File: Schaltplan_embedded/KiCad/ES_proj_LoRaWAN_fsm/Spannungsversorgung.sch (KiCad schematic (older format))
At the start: 37 parts, among them IC1 TLS850B0TBV33ATMA1, IC2 L6924D, IC3 TLS850B0TBV55ATMA1, IC4 SPV1040T, J2 CON-SOCJ-2155, J3 Conn_01x02_Female

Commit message: schaltplan neu
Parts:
- removed R4: 1k, Resistors_SMD:R_0805_HandSoldering, symbol Device:R
- removed R5: 68k, Resistors_SMD:R_0805_HandSoldering, symbol Device:R
- C15: footprint Capacitors_SMD:C_0603_HandSoldering -> Capacitors_SMD:CP_Elec_5x5.3
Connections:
- wire segments 169 -> 162
- no-connect marks 5 -> 6
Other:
- note removed: "Optional! Widerstände können\nevtl. noch weggelassen werden."
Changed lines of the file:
@@
 EESchema Schematic File Version 4
 LIBS:Schaltplan_embedded-cache
-EELAYER 26 0
+EELAYER 30 0
 EELAYER END
 $Descr A4 11693 8268
@@
 F 0 "C15" H 10418 5246 50  0000 L CNN
 F 1 "10uF" H 10418 5155 50  0000 L CNN
-F 2 "Capacitors_SMD:C_0603_HandSoldering" H 10338 5050 50  0001 C CNN
+F 2 "Capacitors_SMD:CP_Elec_5x5.3" H 10338 5050 50  0001 C CNN
 F 3 "~" H 10300 5200 50  0001 C CNN
 	1    10300 5200
@@
 $EndComp
 $Comp
-L Device:R R4
-U 1 1 5DD0CD69
-P 1150 3750
-F 0 "R4" V 943 3750 50  0000 C CNN
-F 1 "1k" V 1034 3750 50  0000 C CNN
-F 2 "Resistors_SMD:R_0805_HandSoldering" V 1080 3750 50  0001 C CNN
-F 3 "~" H 1150 3750 50  0001 C CNN
-	1    1150 3750
-	-1   0    0    1
-$EndComp
-$Comp
-L Device:R R5
-U 1 1 5DD0D292
-P 1150 4150
-F 0 "R5" V 943 4150 50  0000 C CNN
-F 1 "68k" V 1034 4150 50  0000 C CNN
-F 2 "Resistors_SMD:R_0805_HandSoldering" V 1080 4150 50  0001 C CNN
-F 3 "~" H 1150 4150 50  0001 C CNN
-	1    1150 4150
-	-1   0    0    1
-$EndComp
-$Comp
-L power:GND #PWR01
-U 1 1 5DD102DE
-P 1150 4350
-F 0 "#PWR01" H 1150 4100 50  0001 C CNN
-F 1 "GND" H 1155 4177 50  0000 C CNN
-F 2 "" H 1150 4350 50  0001 C CNN
-F 3 "" H 1150 4350 50  0001 C CNN
-	1    1150 4350
-	1    0    0    -1
-$EndComp
-Text GLabel 1050 3550 0    50   Input ~ 0
-VREF
-Wire Wire Line
-	1050 3550 1150 3550
-Wire Wire Line
-	1150 3550 1150 3600
-Wire Wire Line
-	1150 4300 1150 4350
-$Comp
 L Device:R R8
 U 1 1 5DD1CB63
@@
 	1350 4700 1800 4700
 Wire Wire Line
-	1150 3900 1150 3950
-Wire Wire Line
-	2550 3950 2550 4100
-Connection ~ 1150 3950
-Wire Wire Line
-	1150 3950 1150 4000
-Wire Wire Line
 	4950 1300 4950 950
 Wire Wire Line
@@
 	2350 2700 2350 2600
 Connection ~ 2350 2600
-Text Notes 1400 3900 0    50   ~ 0
-Optional! Widerstände können\nevtl. noch weggelassen werden.
-Wire Wire Line
-	1150 3950 2550 3950
 Wire Wire Line
 	3550 4700 3550 4550
@@
 Wire Wire Line
 	1350 1450 1350 1700
+NoConn ~ 2550 4100
 $EndSCHEMATC

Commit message: so
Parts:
- renumbered C16 to C21, C17 to C22, C18 to C23, C19 to C24, C20 to C25, C21 to C26, C22 to C27, C23 to C28, C24 to C29, C12 to C30, C8 to C31, C9 to C32, C13 to C33, C10 to C34, C14 to C35, C11 to C36, C15 to C37, D2 to D3, IC2 to IC4, IC4 to IC5, IC1 to IC6, IC3 to IC7, J2 to J6, J3 to J7, L1 to L4
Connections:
- no-connect marks 6 -> 7

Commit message: neuer Schaltplan
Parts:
- J6: symbol Schaltplan_embedded-rescue:CON-SOCJ-2155-SamacSys_Parts -> Schaltplan_embedded-rescue:CON-SOCJ-2155-SamacSys_Parts-Schaltplan_embedded-rescue
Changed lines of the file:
@@
 	2950 800  2950 1500
 $Comp
-L Schaltplan_embedded-rescue:CON-SOCJ-2155-SamacSys_Parts J6
+L Schaltplan_embedded-rescue:CON-SOCJ-2155-SamacSys_Parts-Schaltplan_embedded-rescue J6
 U 1 1 5DE16150
 P 1200 1250

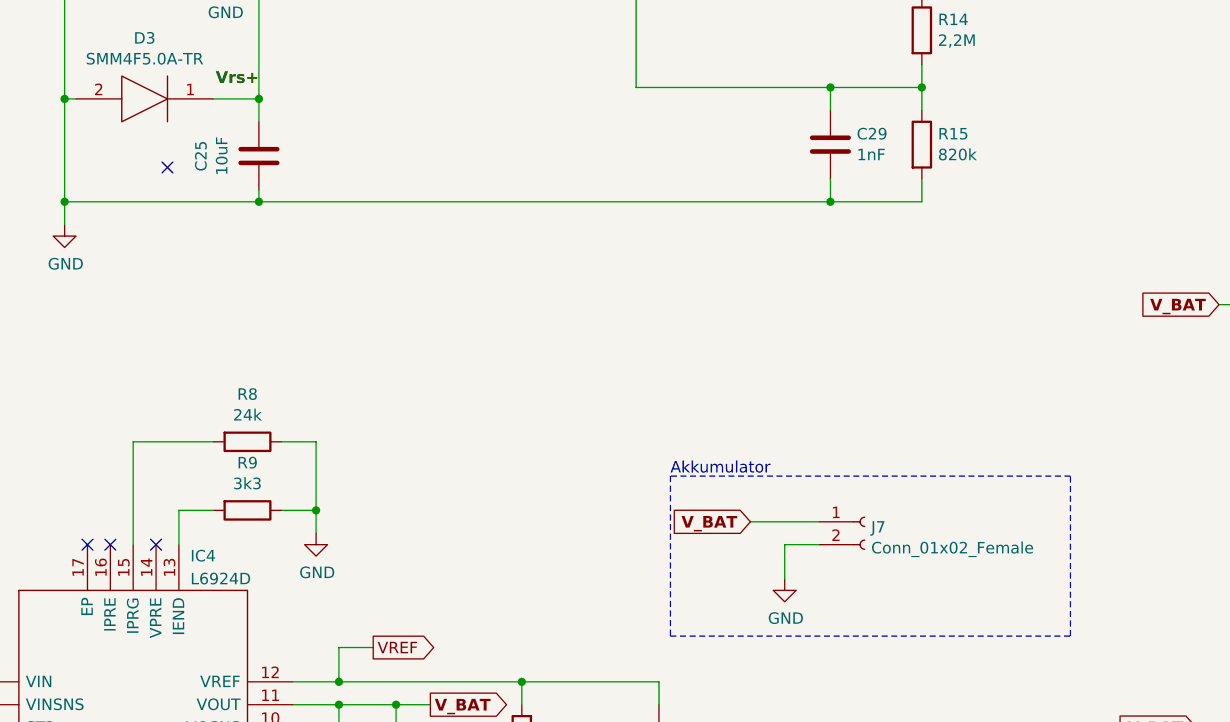
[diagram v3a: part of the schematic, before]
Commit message: Schaltplan  vervollständigt mit Massefläche
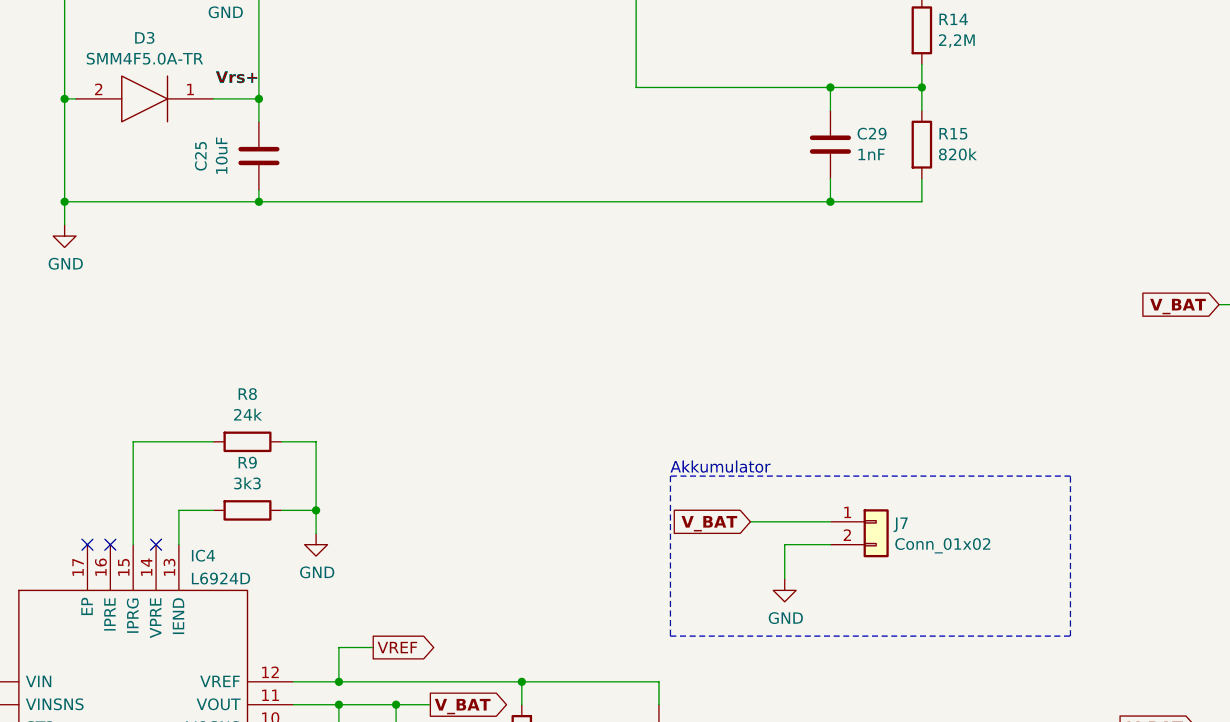
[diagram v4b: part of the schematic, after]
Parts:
- removed J7: Conn_01x02_Female, Pin_Headers:Pin_Header_Straight_1x02_Pitch1.00mm, symbol Connector:Conn_01x02_Female
- added J7: Conn_01x02, Pin_Headers:Pin_Header_Straight_1x02_Pitch2.54mm, symbol Connector_Generic:Conn_01x02
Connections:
- net GND: now also J7.2 (Pin_2)
- net V_BAT: now also J7.1 (Pin_1)
- no-connect marks 7 -> 6
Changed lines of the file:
@@
 Text Notes 10600 7650 0    50   ~ 0
 0.1\n
-$Comp
-L Connector:Conn_01x02_Female J7
-U 1 1 5E182E1C
-P 5850 4000
-F 0 "J7" H 5878 3976 50  0000 L CNN
-F 1 "Conn_01x02_Female" H 5878 3885 50  0000 L CNN
-F 2 "Pin_Headers:Pin_Header_Straight_1x02_Pitch1.00mm" H 5850 4000 50  0001 C CNN
-F 3 "~" H 5850 4000 50  0001 C CNN
-	1    5850 4000
-	1    0    0    -1
-$EndComp
 Text GLabel 5350 4000 0    51   Input ~ 10
 V_BAT
-Wire Wire Line
-	5350 4000 5650 4000
 $Comp
 L power:GND #PWR039
@@
 Wire Wire Line
 	5500 4250 5500 4100
-Wire Wire Line
-	5500 4100 5650 4100
 Wire Notes Line
 	5000 3800 5000 4500
@@
 	1350 1450 1350 1700
 NoConn ~ 2550 4100
-NoConn ~ 2800 2450
+$Comp
+L Connector_Generic:Conn_01x02 J7
+U 1 1 5DF31BD9
+P 5900 4000
+F 0 "J7" H 5980 3992 50  0000 L CNN
+F 1 "Conn_01x02" H 5980 3901 50  0000 L CNN
+F 2 "Pin_Headers:Pin_Header_Straight_1x02_Pitch2.54mm" H 5900 4000 50  0001 C CNN
+F 3 "~" H 5900 4000 50  0001 C CNN
+	1    5900 4000
+	1    0    0    -1
+$EndComp
+Wire Wire Line
+	5350 4000 5700 4000
+Wire Wire Line
+	5500 4100 5700 4100
 $EndSCHEMATC

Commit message: git :)
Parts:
- L4: footprint Resistors_SMD:R_0805_HandSoldering -> Inductor_SMD:L_0805_2012Metric_Pad1.15x1.40mm_HandSolder
- renumbered C21 to C19, C22 to C20, C23 to C21, C24 to C22, C25 to C23, C26 to C24, C27 to C25, C28 to C26, C29 to C27, C30 to C28, C31 to C29, C32 to C30, C33 to C31, C34 to C32, C35 to C33, C36 to C34, C37 to C35, IC4 to IC3, IC5 to IC4, IC6 to IC5, IC7 to IC6, R11 to R10, R12 to R11, R13 to R12, R14 to R13, R15 to R14, R6 to R5, R7 to R6, R8 to R7, R9 to R8, R10 to R9

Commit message: PCB decorations / Gerber Files
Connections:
- net GND: now also IC5.6 (TAB), IC6.6 (TAB)
- no-connect marks 6 -> 4
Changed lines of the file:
@@
 	1    0    0    -1
 $EndComp
-NoConn ~ 9500 3250
-NoConn ~ 9550 5100
 $Comp
 L Device:CP C29
@@
 Wire Wire Line
 	5500 4100 5700 4100
+Wire Wire Line
+	9550 5100 9600 5100
+Wire Wire Line
+	9600 5100 9600 5400
+Wire Wire Line
+	9600 5400 9800 5400
+Wire Wire Line
+	9500 3250 9550 3250
+Wire Wire Line
+	9550 3250 9550 3550
+Wire Wire Line
+	9550 3550 9750 3550
 $EndSCHEMATC

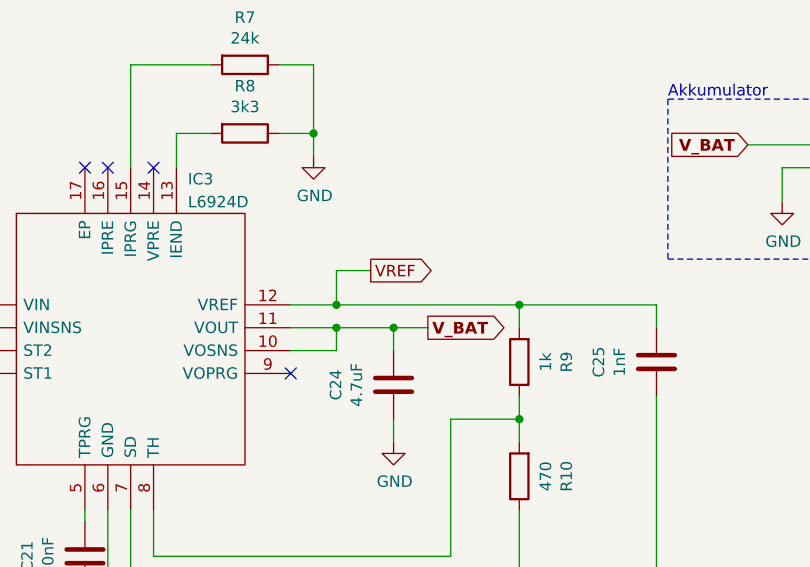
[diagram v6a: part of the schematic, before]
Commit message: Antenna conn change / layout fixes
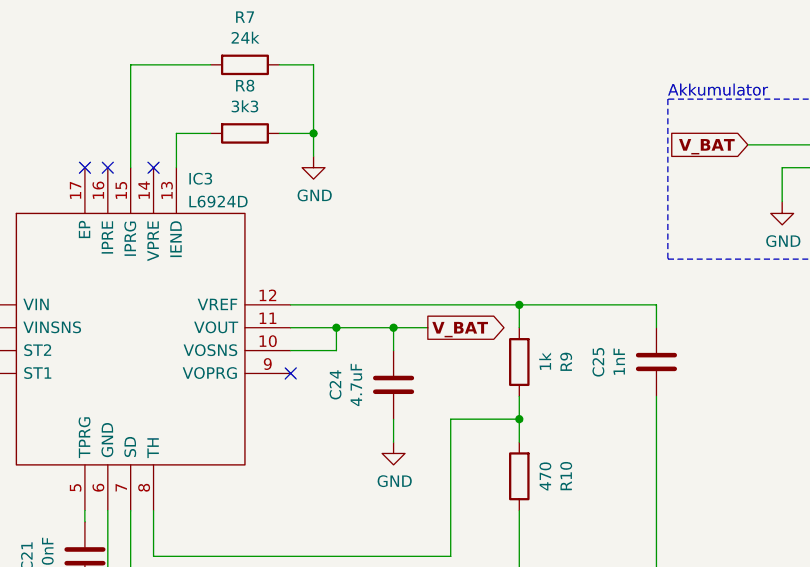
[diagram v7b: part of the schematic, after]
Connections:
- net VREF: no longer names the net of C25.1, IC3.12 (VREF), R9.2
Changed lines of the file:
@@
 	4350 5100 4350 5200
-Wire Wire Line
-	3350 4700 3550 4700
 Wire Wire Line
 	4350 4700 4350 4800
@@
 Wire Wire Line
 	3050 1400 3050 1600
-Text GLabel 3700 4550 2    50   Output ~ 0
-VREF
 Wire Wire Line
 	2350 1700 2350 2150
@@
 	2350 2700 2350 2600
 Connection ~ 2350 2600
-Wire Wire Line
-	3550 4700 3550 4550
-Wire Wire Line
-	3550 4550 3700 4550
-Connection ~ 3550 4700
-Wire Wire Line
-	3550 4700 4350 4700
 Text Notes 7350 7500 0    50   ~ 0
 Spannungsversorgung
@@
 Wire Wire Line
 	9550 3550 9750 3550
+Wire Wire Line
+	3350 4700 4350 4700
 $EndSCHEMATC
